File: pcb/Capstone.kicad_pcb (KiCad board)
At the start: 4 copper layers, 90 x 35 mm, 109 parts, among them IC1 HSFPAR004A, IC2 HSFPAR004A, IC3 HSFPAR004A, IC4 HSFPAR004A, J1 Conn_01x14_Socket, J2 Conn_01x14_Socket, J3 Conn_01x12_Socket, P1 USB_C_Plug_USB2.0, Q1 SS8050, Q2 SS8050, SW1 SW_Push, SW2 SW_Push, U1 ADS1015IDGS, U10 INA333xxDGK, U11 BMM350, U12 ICM-42688-P, U13 ICM-42688-P, U14 TLV75718PDBV, U2 ESP32-S3-WROOM-1, U3 TLV75733PDBV, U4 USBLC6-2SC6, U5 CP2102N-Axx-xQFN28, U6 INA333xxDGK, U7 ADS1015IDGS, U8 INA333xxDGK, U9 INA333xxDGK

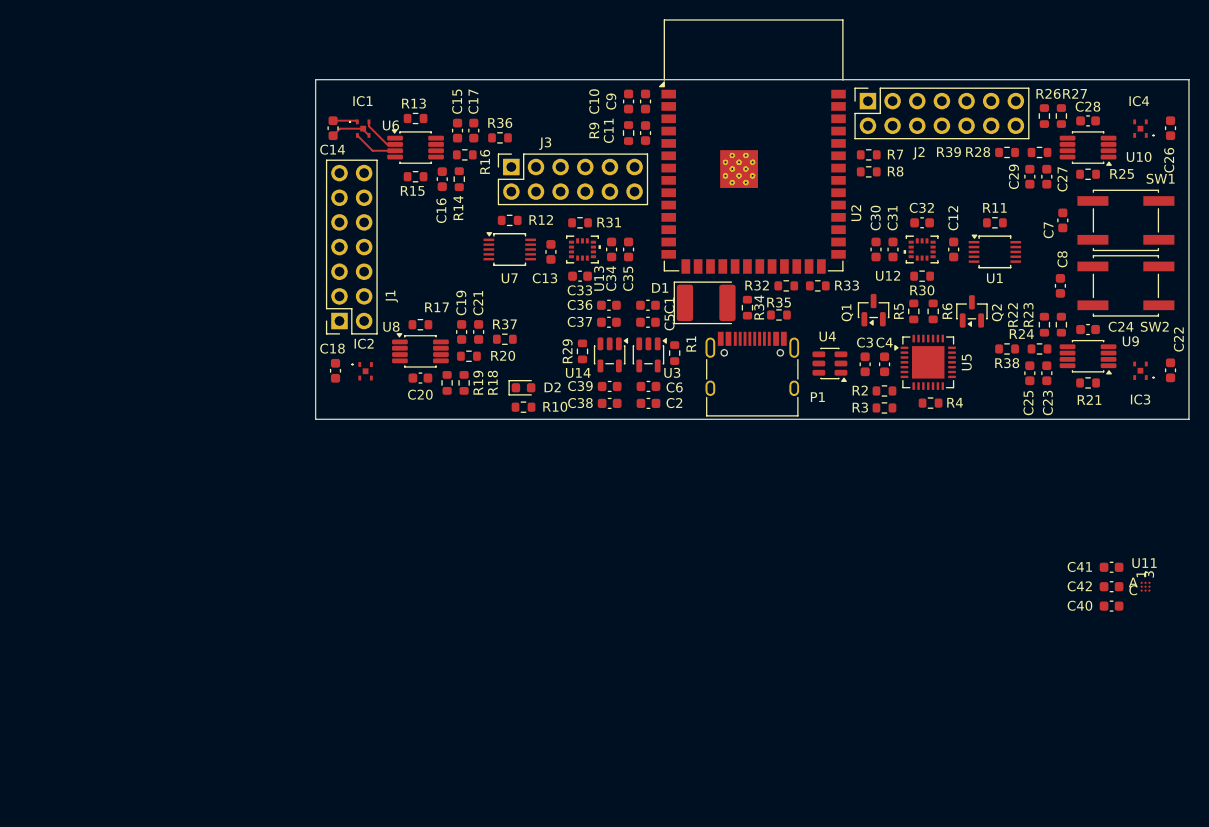
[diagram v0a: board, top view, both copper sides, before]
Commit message: Connect components on PCB
Add electronic connections for printed circuit board components.
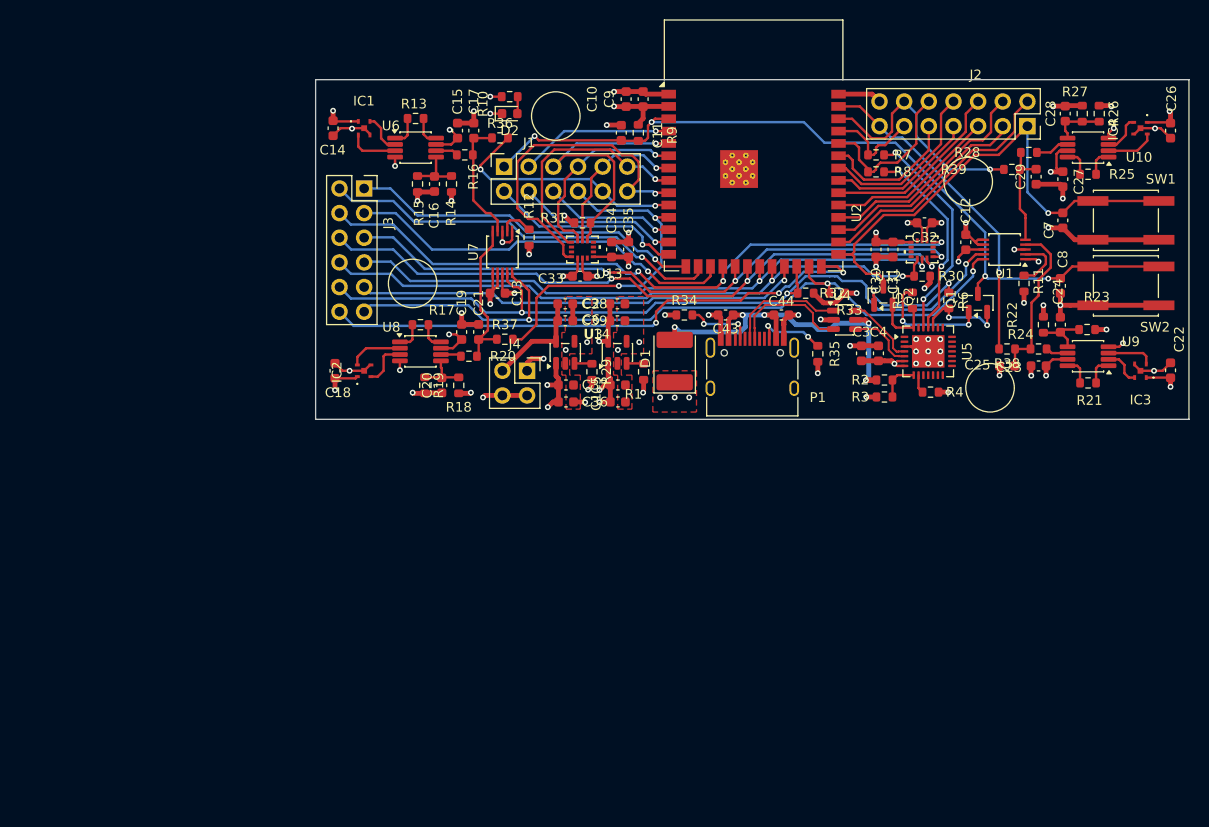
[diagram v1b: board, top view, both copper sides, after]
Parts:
- removed C40, C41: 0.1u, Capacitor_SMD:C_0603_1608Metric
- removed C42: 2.2u, Capacitor_SMD:C_0603_1608Metric
- removed U11: BMM350, BMM350:BGA9_BMM350_BOS
- added C43: 10n, Capacitor_SMD:C_0603_1608Metric, F.Cu at (177.8, 74.2)
- added C44: 10n, Capacitor_SMD:C_0603_1608Metric, F.Cu at (183.5, 74.2)
- added J4: Conn_01x04_Socket, Connector_PinSocket_2.54mm:PinSocket_2x02_P2.54mm_Vertical, F.Cu at (157.3, 80.0)
- J1: value Conn_01x14_Socket -> Conn_01x12_Socket; footprint Connector_PinSocket_2.54mm:PinSocket_2x07_P2.54mm_Vertical -> Connector_PinSocket_2.54mm:PinSocket_2x06_P2.54mm_Vertical
- moved R10 32.0 mm to (155.5, 51.8)
- moved D2 28.3 mm to (155.5, 53.5)
- moved J1 23.3 mm to (154.9, 59.0), turned to 90 degrees
- moved J2 16.6 mm to (208.8, 54.8), turned to -90 degrees
- moved J3 15.3 mm to (140.5, 61.2), turned to 0 degrees
- moved C38 11.2 mm to (161.2, 73.1), turned to 0 degrees
- moved C36 10.9 mm to (161.3, 83.2), turned to 0 degrees
- moved Q1 10.8 mm to (203.8, 73.0)
- moved C2 10.7 mm to (166.6, 73.1), turned to 0 degrees
- moved C1 10.4 mm to (166.7, 83.2), turned to 0 degrees
- moved Q2 9.27 mm to (194.0, 72.2)
- moved C39 8.16 mm to (161.2, 74.8), turned to 0 degrees
- moved C37 7.83 mm to (161.3, 81.5), turned to 0 degrees
- moved C6 7.48 mm to (166.6, 74.8), turned to 0 degrees
- moved C5 7.17 mm to (166.7, 81.5), turned to 0 degrees
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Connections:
- net Net-(IC1-V1) renamed /F0_P
- net Net-(IC1-V2) renamed /F0_N
- net Net-(IC2-V1) renamed /F1_P
- net Net-(IC2-V2) renamed /F1_N
- net Net-(IC3-V1) renamed /F2_P
- net Net-(IC3-V2) renamed /F2_N
- net Net-(IC4-V1) renamed /F3_P
- net Net-(IC4-V2) renamed /F3_N
- C7 pad 2: /IO1 -> /IO0
- J1 pad 1: GND -> /EN
- J1 pad 11: /IO18 -> /SDO1
- J1 pad 12: /IO8 -> /INT_IMU1
- J1 pad 2: VCC_3V3 -> /USB_D+
- J1 pad 3: /EN -> /INT_MAG1
- J1 pad 4: /INT_MAG1 -> /USB_D-
- J1 pad 6: /SDI1 -> /IO8
- J1 pad 7: /SCK1 -> /SDI1
- J1 pad 8: /SDO1 -> /IO18
- J1 pad 9: /INT_IMU1 -> /SCK1
- J3 pad 4: /CS0 -> /INT_IMU0
- J3 pad 5: /SDI0 -> /SDO0
- J3 pad 6: /SCK0 -> /SDI0
- J3 pad 7: /SDO0 -> /SCK0
- J3 pad 8: /INT_IMU0 -> /CS0
- P1 pad A6: Net-(P1-D+) -> /USB_DI_P
- P1 pad A7: Net-(P1-D-) -> /USB_DI_N
- R36 pad 1: /IO1 -> /IO17
- R37 pad 1: /IO2 -> /IO18
- R38 pad 1: /IO17 -> /IO1
- R39 pad 1: /IO18 -> /IO2
- SW1 pad 2: /IO1 -> /IO0
- U14 pad 4: unconnected-(U14-NC-Pad4) -> GND
- U2 pad 18: /CS0 -> /INT_IMU0
- U2 pad 19: /SDI0 -> /SDO0
- U2 pad 20: /SCK0 -> /SDI0
- U2 pad 21: /SDO0 -> /SCK0
- U2 pad 22: /INT_IMU0 -> /CS0
- U3 pad 4: unconnected-(U3-NC-Pad4) -> GND
- U4 pad 1: Net-(P1-D-) -> /USB_DI_P
- U4 pad 2: unconnected-(U4-GND-Pad2) -> GND
- U4 pad 3: Net-(P1-D+) -> /USB_DI_N
- U4 pad 4: /USB_D_P -> /USB_D_N
- U4 pad 6: /USB_D_N -> /USB_D_P
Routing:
- net GND: track 4.35 -> 132.6 mm, vias 0 -> 52
- net VCC_3V3: track 2.55 -> 91.6 mm, vias 0 -> 30
- net /EN: track 0.00 -> 84.4 mm, vias 0 -> 4
- net /SDA: track 0.00 -> 83.2 mm, vias 0 -> 3
- net /SCL: track 0.00 -> 81.2 mm, vias 0 -> 3
- net /INT_IMU0: track 0.00 -> 70.2 mm, vias 0 -> 3
- net /SDI0: track 0.00 -> 68.8 mm, vias 0 -> 3
- net /SDO0: track 0.00 -> 66.4 mm, vias 0 -> 3
- net /CS0: track 0.00 -> 66.0 mm, vias 0 -> 2
- net /SCK0: track 0.00 -> 63.0 mm, vias 0 -> 2
- net /IO45: track 0.00 -> 58.1 mm, vias 0 -> 3
- net /IO0: track 0.00 -> 52.5 mm, vias 0 -> 1
- net /IO21: track 0.00 -> 46.4 mm, vias 0 -> 1
- net /IO46: track 0.00 -> 41.8 mm, vias 0 -> 1
- net VBUS: track 0.00 -> 41.1 mm, vias 0 -> 5
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- added copper zone on F.Cu, net GND
- added copper zone on In2.Cu, net GND
- added copper zone on In1.Cu, net VCC_3V3
- added copper zone on F.Cu, net VCC_5V
- added copper zone on In1.Cu, net VCC_5V

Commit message: Revise PCB for procurement
Revise printed circuit board with feedback from industry sponsor. Final design to send to JLCPCB.

 - Add Gerber files

 - Add Component Placement List and position files
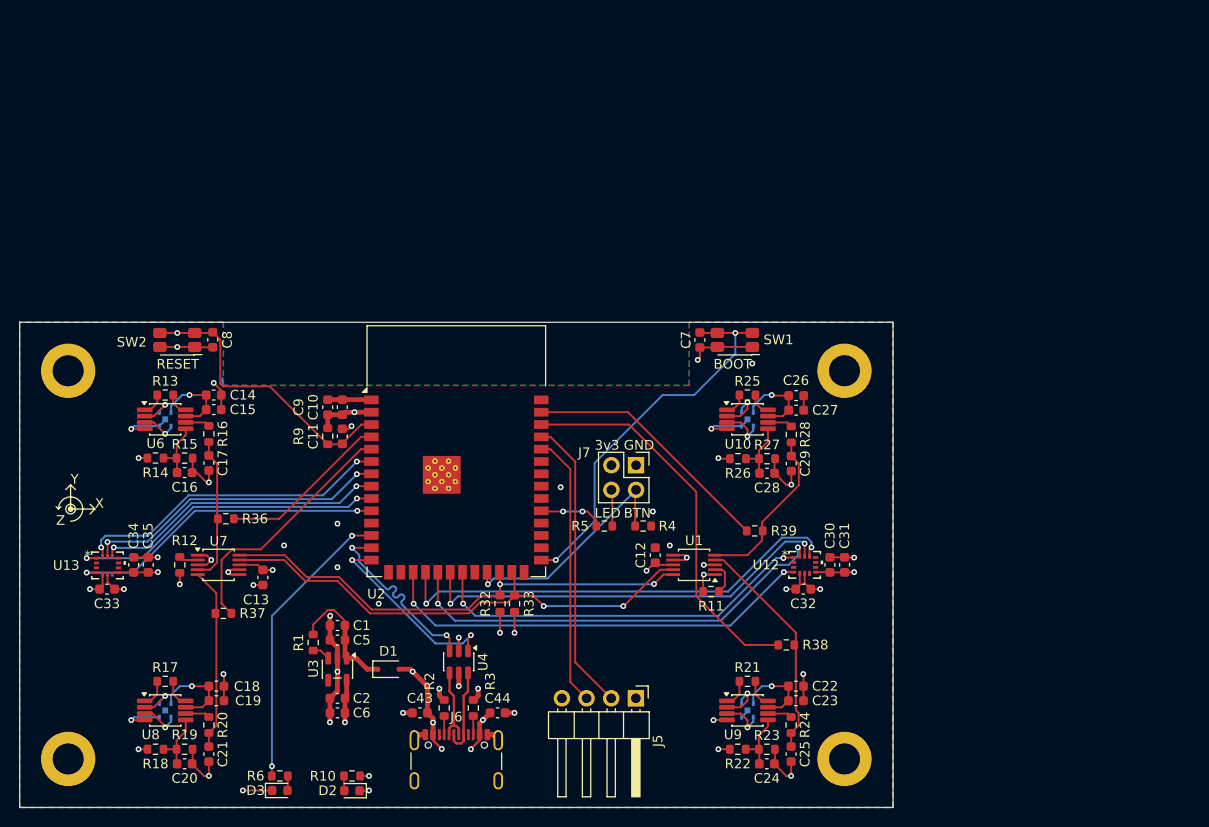
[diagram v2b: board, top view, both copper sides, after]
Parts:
- removed C3: 4.7u, Capacitor_SMD:C_0603_1608Metric
- removed C36, C38: 10u, Capacitor_SMD:C_0603_1608Metric
- removed C37, C39, C4: 0.1u, Capacitor_SMD:C_0603_1608Metric
- removed P1: USB_C_Plug_USB2.0, Connector_USB:USB_C_Receptacle_HRO_TYPE-C-31-M-12
- removed Q1, Q2: SS8050, Package_TO_SOT_SMD:SOT-23
- removed R29: 10k, Resistor_SMD:R_0603_1608Metric
- removed R30, R31: 4k7, Resistor_SMD:R_0603_1608Metric
- removed R34, R35: 5k1, Resistor_SMD:R_0603_1608Metric
- removed R7, R8: 0, Resistor_SMD:R_0603_1608Metric
- removed U14: TLV75718PDBV, Package_TO_SOT_SMD:SOT-23-5
- removed U5: CP2102N-Axx-xQFN28, Package_DFN_QFN:QFN-28-1EP_5x5mm_P0.5mm_EP3.35x3.35mm
- added D3: LED (AMBER), LED_SMD:LED_0603_1608Metric, F.Cu at (131.8, 123.2)
- added J5: Conn_01x02, Connector_PinHeader_2.54mm:PinHeader_1x04_P2.54mm_Horizontal, F.Cu at (168.5, 113.8)
- added J6: USB_C_Receptacle, Connector_USB:USB_C_Receptacle_GCT_USB4105-xx-A_16P_TopMnt_Horizontal, F.Cu at (150.0, 121.2)
- added J7: Conn_02x02_Counter_Clockwise, Connector_PinSocket_2.54mm:PinSocket_2x02_P2.54mm_Vertical, F.Cu at (168.5, 89.7)
- C31, C35: value 2.2u -> 2.2u +/- 10% X7R
- C32, C33: value 10n -> 10n +/- 10% X7R
- C9: value 10u -> 22u
- D1: value D_Schottky -> D_Schottky BAT760; footprint Diode_SMD:D_2114_3652Metric -> Diode_SMD:D_SOD-323F
- D2: value LED -> LED (RED)
- IC1, IC2, IC3, IC4: moved to B.Cu
- J1, J3: value Conn_01x12_Socket -> Conn_01x01; footprint Connector_PinSocket_2.54mm:PinSocket_2x06_P2.54mm_Vertical -> MountingHole:MountingHole_3.2mm_M3_DIN965_Pad
- J2: value Conn_01x14_Socket -> Conn_01x01; footprint Connector_PinSocket_2.54mm:PinSocket_2x07_P2.54mm_Vertical -> MountingHole:MountingHole_3.2mm_M3_DIN965_Pad
- J4: value Conn_01x04_Socket -> Conn_01x01; footprint Connector_PinSocket_2.54mm:PinSocket_2x02_P2.54mm_Vertical -> MountingHole:MountingHole_3.2mm_M3_DIN965_Pad
- R13, R17, R21: value 499 -> 6.49 +/- 1%
- R14, R18, R22, R26: value 10k -> 10k +/- 1%
- R15, R19, R23, R27: value 3k -> 3k +/- 1%
- R2: value 22k1 -> 5.1k
- R25: value 499 -> 6.49k +/- 1%
- R3: value 47k5 -> 5.1k
- R4: value 1k -> 10k
- R5: value 10k -> 100
- R6: value 10k -> 220
- SW1, SW2: footprint Button_Switch_SMD:SW_SPST_EVQQ2 -> Button_Switch_SMD:SW_SPST_EVQP7A
- moved J2 118.4 mm to (110.0, 120.0), turned to 0 degrees
- moved SW2 97.9 mm to (121.2, 76.8)
- moved C8 87.5 mm to (124.9, 76.8)
- moved R6 84.6 mm to (131.8, 121.8), turned to 180 degrees
- moved R10 71.9 mm to (139.2, 121.8), turned to 180 degrees
- moved D2 71.6 mm to (139.2, 123.3), turned to 180 degrees
- moved C35 59.2 mm to (118.2, 100.0)
- moved C34 59.0 mm to (116.8, 100.0)
- moved U13 58.8 mm to (114.1, 100.1)
- moved C33 58.5 mm to (114.0, 102.5)
- moved R2 56.6 mm to (148.8, 114.8), turned to 90 degrees
- moved C24 54.4 mm to (182.0, 120.5), turned to 0 degrees
- moved R23 54.4 mm to (182.0, 119.0)
- moved R22 53.9 mm to (179.0, 119.0), turned to 0 degrees
- moved IC3 53.5 mm to (180.0, 115.0)
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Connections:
- J1 pad 1: /EN -> GND
- J2 pad 1: /IO0 -> GND
- J3 pad 1: /IO3 -> GND
- J4 pad 1: VCC_3V3 -> GND
- R2 pad 1: VBUS -> /CC1
- R2 pad 2: Net-(U5-VBUS) -> GND
- R3 pad 1: GND -> /CC2
- R3 pad 2: Net-(U5-VBUS) -> GND
- R32 pad 1: /SDA -> /SCL
- R33 pad 1: /SCL -> /SDA
- R36 pad 1: /IO17 -> /F0_d
- R37 pad 1: /IO18 -> /F1_d
- R38 pad 1: /IO1 -> /F2_d
- R39 pad 1: /IO2 -> /F3_d
- R4 pad 1: Net-(U5-~{RST}) -> /EXT_BTN
- R4 pad 2: VCC_3V3 -> GND
- R5 pad 2: /DTR -> /EXT_LED
- R6 pad 1: /RTS -> Net-(D3-A)
- R6 pad 2: Net-(Q2-B) -> /STATUS_LED
- U12 pad 1: /SDO0 -> /CONTROLLER_SDI_IMU0
- U12 pad 12: /CS0 -> /CS_IMU0
- U12 pad 13: /SCK0 -> /CLK_IMU0
- U12 pad 14: /SDI0 -> /CONTROLLER_SDO_IMU0
- U13 pad 1: /SDO1 -> /CONTROLLER_SDI_IMU1
- U13 pad 12: /CS1 -> /CS_IMU1
- U13 pad 13: /SCK1 -> /CLK_IMU1
- U13 pad 14: /SDI1 -> /CONTROLLER_SDO_IMU1
- U2 pad 10: /IO17 -> /INT_IMU1
- U2 pad 11: /IO18 -> unconnected-(U2-IO18-Pad11)
- U2 pad 12: /IO8 -> /STATUS_LED
- U2 pad 13: /USB_D- -> /USB_D_N
- U2 pad 14: /USB_D+ -> /USB_D_P
- U2 pad 15: /IO3 -> unconnected-(U2-IO3-Pad15)
- U2 pad 16: /IO46 -> unconnected-(U2-IO46-Pad16)
- U2 pad 17: /IO9 -> /INT_IMU0
- U2 pad 18: /INT_IMU0 -> /CS_IMU0
- U2 pad 19: /SDO0 -> /CONTROLLER_SDO_IMU0
- U2 pad 20: /SDI0 -> /CLK_IMU0
- U2 pad 21: /SCK0 -> /CONTROLLER_SDI_IMU0
- U2 pad 22: /CS0 -> unconnected-(U2-IO14-Pad22)
- U2 pad 23: /IO21 -> /EXT_BTN
- U2 pad 24: /SDA -> /SCL
- U2 pad 25: /SCL -> /SDA
- U2 pad 26: /IO45 -> unconnected-(U2-IO45-Pad26)
- U2 pad 28: /IO35 -> unconnected-(U2-IO35-Pad28)
- U2 pad 29: /IO36 -> unconnected-(U2-IO36-Pad29)
- U2 pad 30: /IO37 -> unconnected-(U2-IO37-Pad30)
- U2 pad 31: /IO38 -> /EXT_LED
- U2 pad 32: /IO39 -> unconnected-(U2-IO39-Pad32)
- U2 pad 33: /IO40 -> unconnected-(U2-IO40-Pad33)
- U2 pad 34: /IO41 -> unconnected-(U2-IO41-Pad34)
- U2 pad 35: /IO42 -> unconnected-(U2-IO42-Pad35)
- U2 pad 38: /IO2 -> /F2_d
- U2 pad 39: /IO1 -> /F3_d
- U2 pad 4: /INT_MAG1 -> /F0_d
- U2 pad 5: /CS1 -> /F1_d
- U2 pad 6: /SDI1 -> /CONTROLLER_SDO_IMU1
- U2 pad 7: /SCK1 -> /CLK_IMU1
- U2 pad 8: /SDO1 -> /CS_IMU1
- U2 pad 9: /INT_IMU1 -> /CONTROLLER_SDI_IMU1
- U3 pad 4: GND -> unconnected-(U3-NC-Pad4)
- U4 pad 1: /USB_DI_P -> /USB_D_P
- U4 pad 3: /USB_DI_N -> /USB_D_N
- U4 pad 4: /USB_D_N -> /USB_D-
- U4 pad 6: /USB_D_P -> /USB_D+
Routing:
- net /SDI0: track 68.8 -> 0.00 mm, vias 3 -> 0
- net /SDO0: track 66.4 -> 0.00 mm, vias 3 -> 0
- net /CS0: track 66.0 -> 0.00 mm, vias 2 -> 0
- net /SCK0: track 63.0 -> 0.00 mm, vias 2 -> 0
- net /IO45: track 58.1 -> 0.00 mm, vias 3 -> 0
- net /EN: track 84.4 -> 30.9 mm, vias 4 -> 1
- net /CS_IMU0: track 0.00 -> 47.5 mm, vias 0 -> 2
- net /IO21: track 46.4 -> 0.00 mm, vias 1 -> 0
- net /CONTROLLER_SDO_IMU0: track 0.00 -> 45.7 mm, vias 0 -> 2
- net /CLK_IMU0: track 0.00 -> 43.8 mm, vias 0 -> 2
- net /IO46: track 41.8 -> 0.00 mm, vias 1 -> 0
- net /IO9: track 40.6 -> 0.00 mm, vias 1 -> 0
- net /CONTROLLER_SDI_IMU0: track 0.00 -> 40.3 mm, vias 0 -> 2
- net /F2_d: track 0.00 -> 40.1 mm
- net /IO3: track 36.5 -> 0.00 mm, vias 1 -> 0
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- added copper zone on B.Cu, net GND
- added copper zone on In1.Cu, net GND
- added copper zone on In2.Cu, net VBUS
- added copper zone on In2.Cu, net VCC_3V3
- removed copper zone on In2.Cu, net GND
- removed copper zone on In1.Cu, net VCC_3V3
- removed copper zone on F.Cu, net VCC_5V
- removed copper zone on In1.Cu, net VCC_5V
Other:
- board size 90 x 35 mm -> 90 x 50 mm
- board text added: "3v3"
- board text added: "Acculux v0.1"
- board text added: "BOOT"
- board text added: "BTN"
- board text added: "GND"
- board text added: "LED"
- board text added: "RESET"
- board text added: "X"
- board text added: "Y"
- board text added: "Z"
